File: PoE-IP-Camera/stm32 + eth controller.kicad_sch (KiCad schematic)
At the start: 45 parts, among them J3 Conn_01x0, J4 Conn_01x04_Socket, J5 Conn_01x04_Socket, SW2 434133025816, U5 STM32F030F4Px, Y1 X322525MOB4SI, Y2 X322525MOB4SI

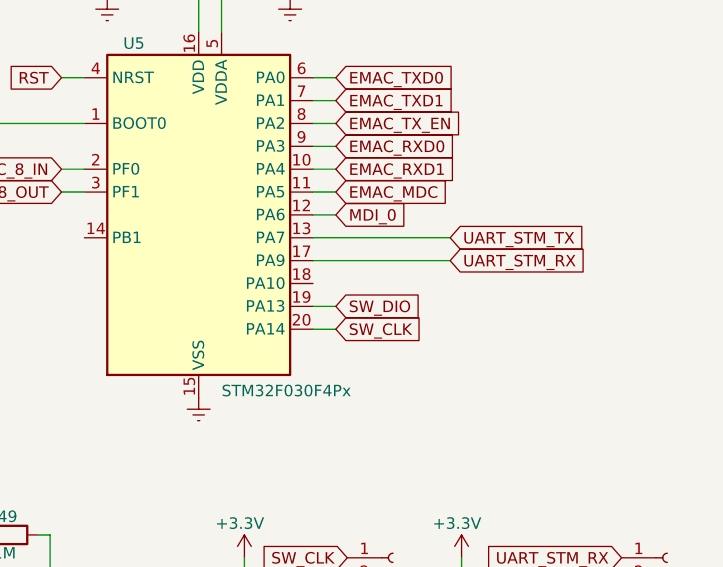
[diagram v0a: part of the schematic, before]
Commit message: частичная трассировка
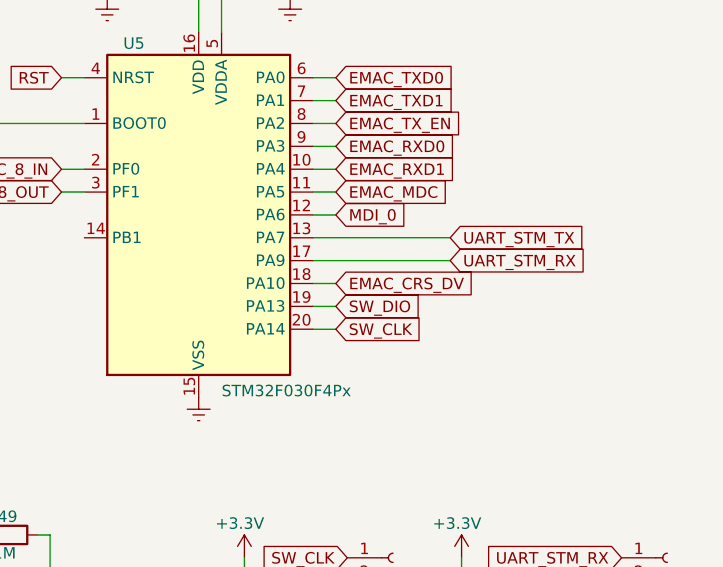
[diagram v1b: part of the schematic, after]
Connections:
- net EMAC_CRS_DV: now also U5.18 (PA10)
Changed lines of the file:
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@@
 	(wire
 		(pts
+			(xy 233.68 74.93) (xy 231.14 74.93)
+		)
+		(stroke
+			(width 0)
+			(type default)
+		)
+	)
+	(wire
+		(pts
 			(xy 210.82 35.56) (xy 208.28 35.56)
 		)
@@
 			(effects
 				(font
+					(size 1.27 1.27)
+				)
+				(justify left)
+				(hide yes)
+			)
+		)
+	)
+	(global_label "EMAC_CRS_DV"
+		(shape input)
+		(at 233.68 74.93 0)
+		(fields_autoplaced yes)
+		(effects
+			(font
+				(size 1.27 1.27)
+			)
+			(justify left)
+		)
+		(property "Intersheetrefs" "${INTERSHEET_REFS}"
+			(at 249.6675 74.93 0)
+			(effects
+				(font

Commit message: чут чут трассировки
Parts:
- renumbered R35 to R36, R36 to R37, R37 to R38, R38 to R39, R39 to R40, R40 to R41, R41 to R42, R42 to R43, R43 to R44, R44 to R45, R45 to R46, R46 to R47, R47 to R48, R48 to R49, R49 to R50
